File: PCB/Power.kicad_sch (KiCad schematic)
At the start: 23 parts, among them J9 USB_C_Receptacle_USB2.0_16P, SW2 SW_Push, U1 TLV62569ADRL, U4 CP2102N-Axx-xQFN28

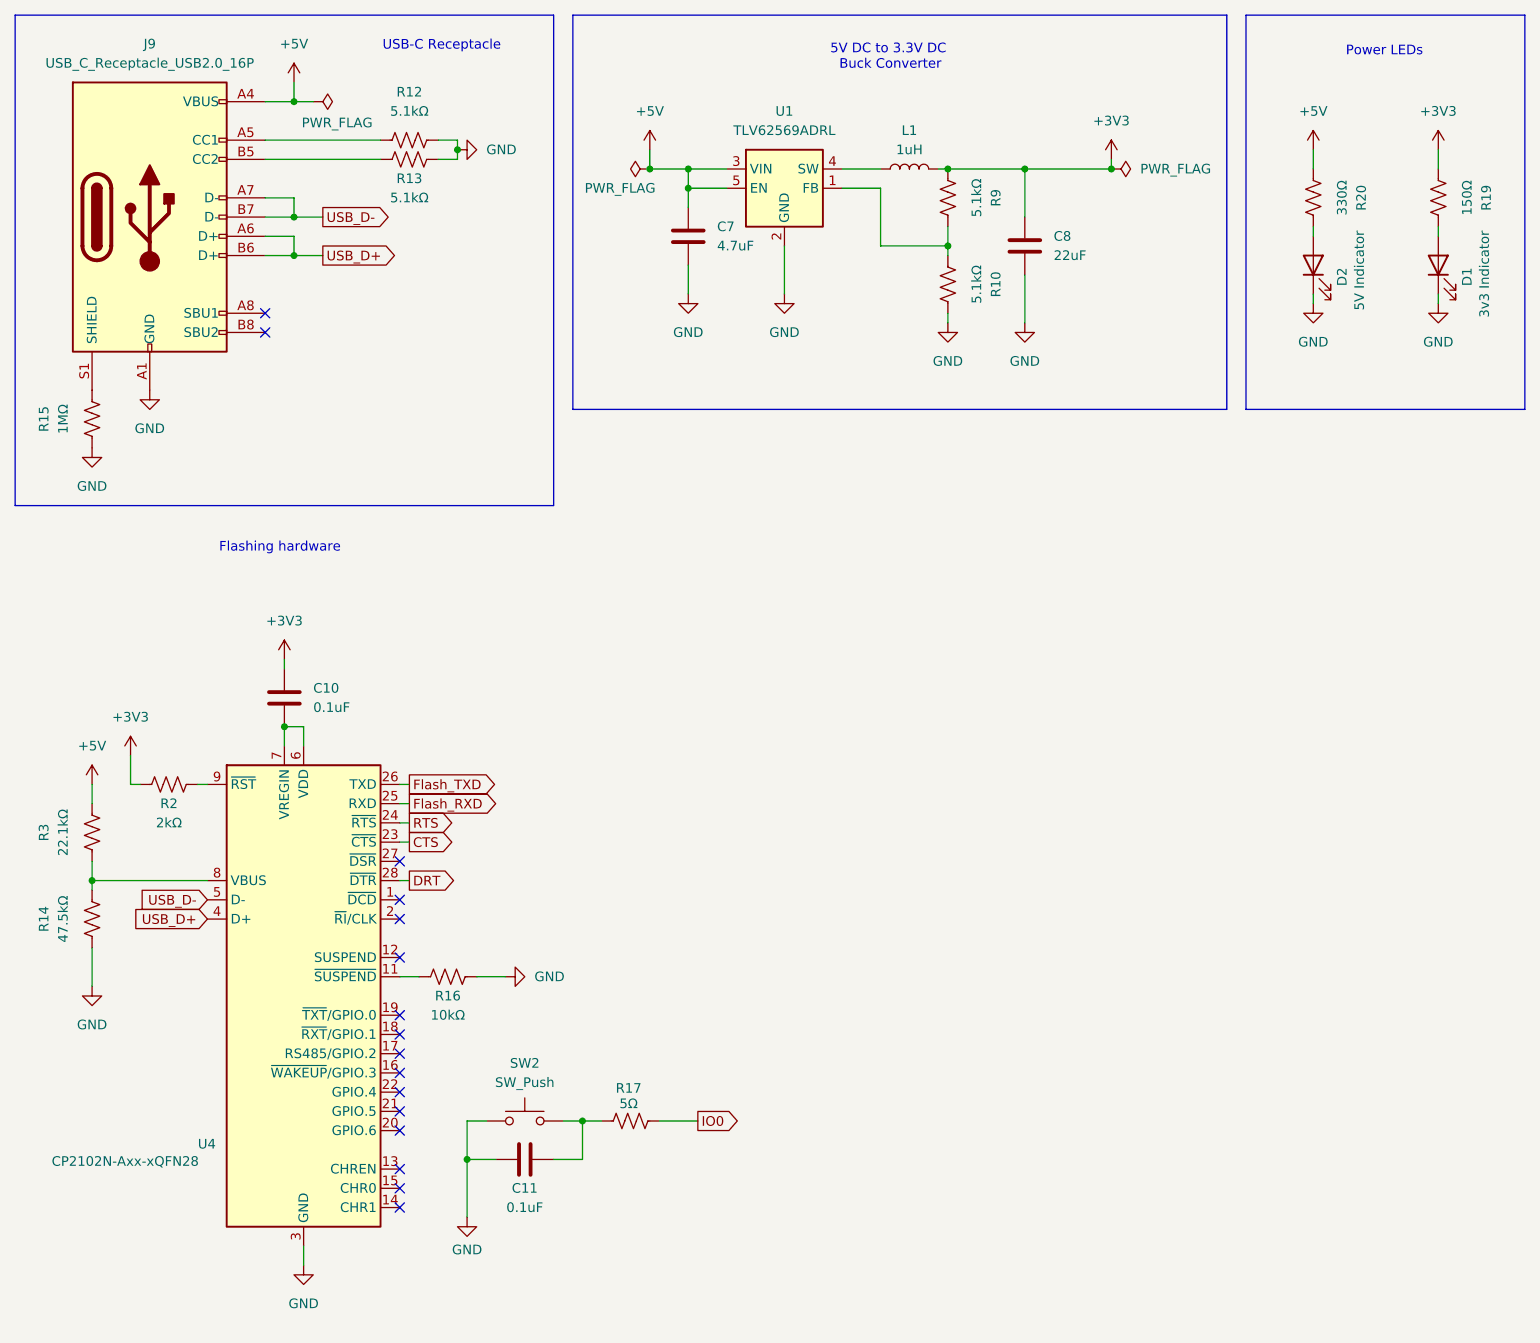
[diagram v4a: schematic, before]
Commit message: add esd protection and buck caps and move USB-C over edge
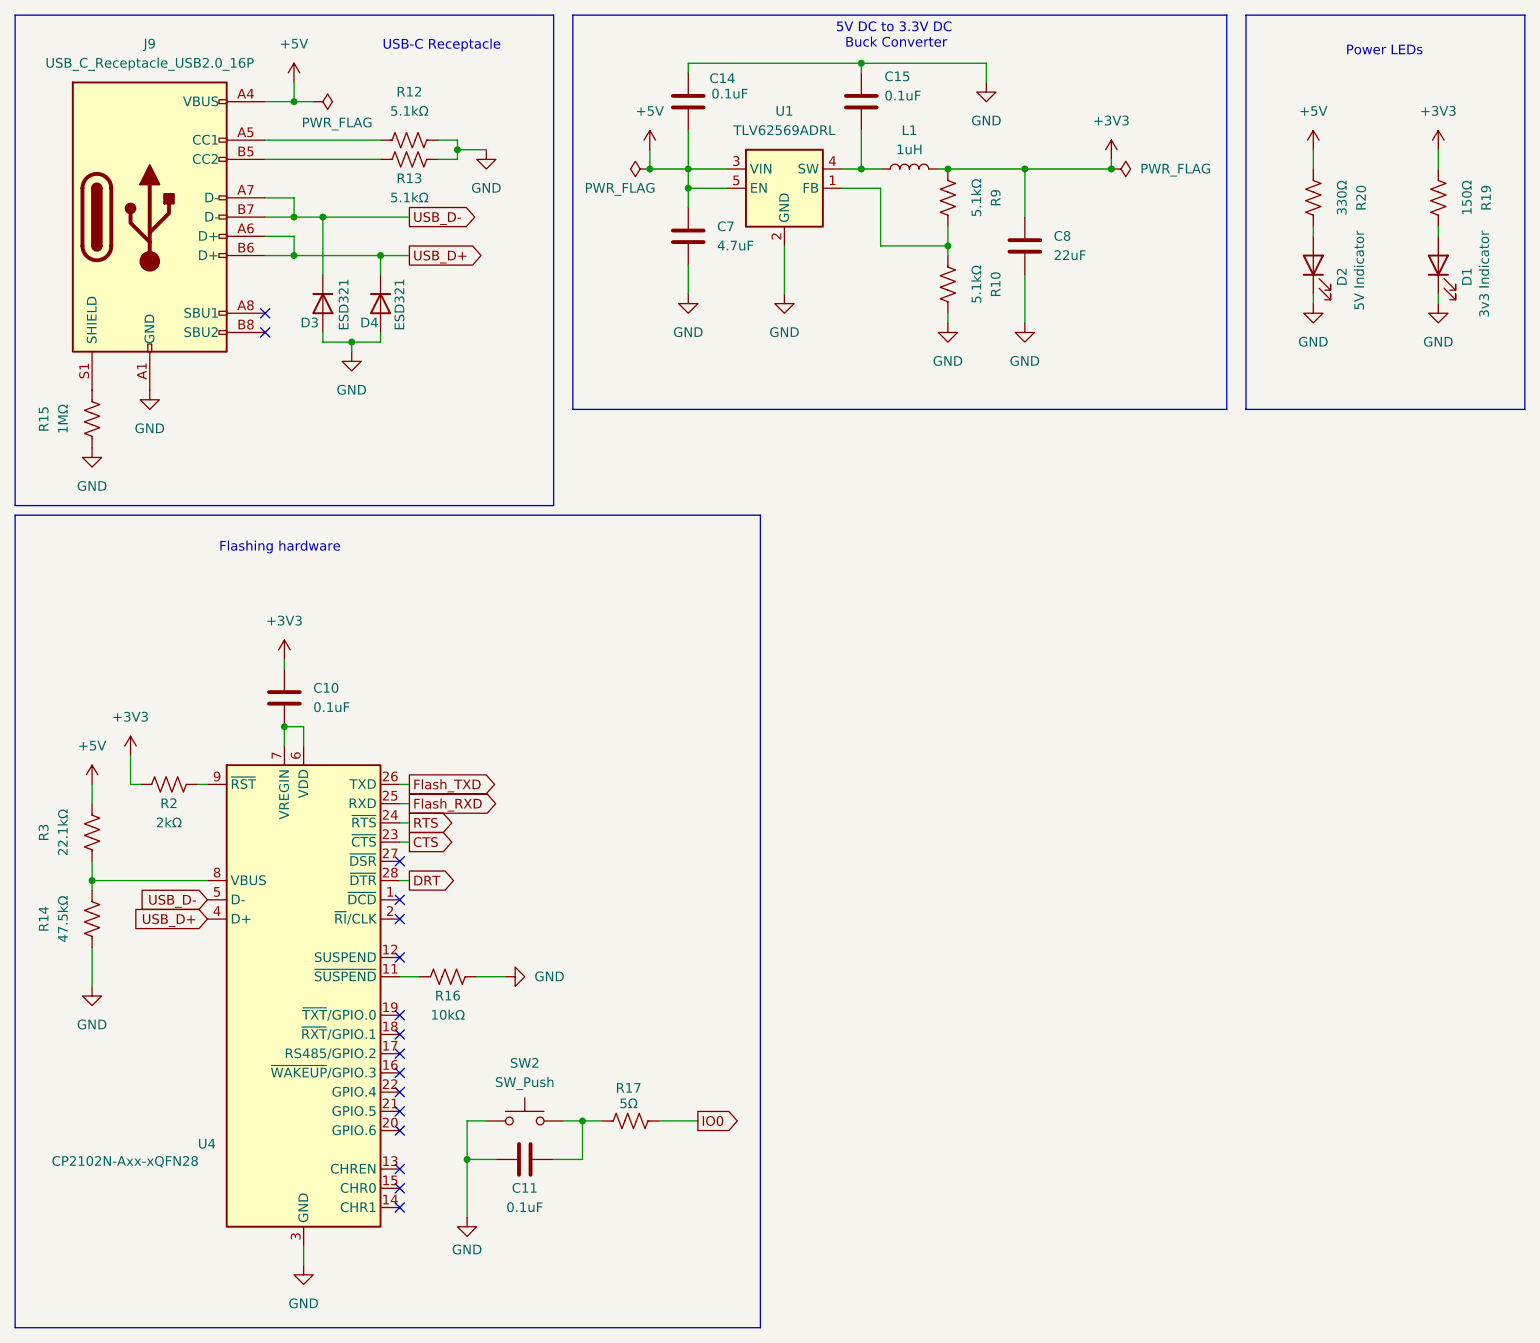
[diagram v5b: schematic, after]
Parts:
- added C14, C15: 0.1uF, Capacitor_SMD:C_1206_3216Metric_Pad1.33x1.80mm_HandSolder, symbol Device:C
- added D3, D4: ESD321, Diode_SMD:D_01005_0402Metric_Pad0.57x0.30mm_HandSolder, symbol Device:D
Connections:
- net +5V: now also C14.2
- net GND: now also C14.1, C15.1, D3.2 (A), D4.2 (A)
- net USB_D+: now also D4.1 (K)
- net USB_D-: now also D3.1 (K)
- net at L1.1, U1.4 (SW): now also C15.2

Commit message: fix esd diode footprints
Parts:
- D3, D4: footprint Diode_SMD:D_01005_0402Metric_Pad0.57x0.30mm_HandSolder -> Diode_SMD:D_0402_1005Metric_Pad0.77x0.64mm_HandSolder
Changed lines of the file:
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@@
 			)
 		)
-		(property "Footprint" "Diode_SMD:D_01005_0402Metric_Pad0.57x0.30mm_HandSolder"
+		(property "Footprint" "Diode_SMD:D_0402_1005Metric_Pad0.77x0.64mm_HandSolder"
 			(at 54.61 52.07 0)
 			(effects
@@
 			)
 		)
-		(property "Footprint" "Diode_SMD:D_01005_0402Metric_Pad0.57x0.30mm_HandSolder"
+		(property "Footprint" "Diode_SMD:D_0402_1005Metric_Pad0.77x0.64mm_HandSolder"
 			(at 62.23 52.07 0)
 			(effects

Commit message: Start of feedback implementation
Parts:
- removed C10, C11, C14, C15: 0.1uF, Capacitor_SMD:C_1206_3216Metric_Pad1.33x1.80mm_HandSolder, symbol Device:C
- removed R14: 47.5kΩ, Resistor_SMD:R_1206_3216Metric_Pad1.30x1.75mm_HandSolder, symbol Device:R_US
- removed R16: 10kΩ, Resistor_SMD:R_1206_3216Metric_Pad1.30x1.75mm_HandSolder, symbol Device:R_US
- removed R17: 5Ω, Resistor_SMD:R_1206_3216Metric_Pad1.30x1.75mm_HandSolder, symbol Device:R_US
- removed R2: 2kΩ, Resistor_SMD:R_1206_3216Metric_Pad1.30x1.75mm_HandSolder, symbol Device:R_US
- removed R3: 22.1kΩ, Resistor_SMD:R_1206_3216Metric_Pad1.30x1.75mm_HandSolder, symbol Device:R_US
- removed SW2: SW_Push, SMD_Button:Shop_SMD_Button, symbol Switch:SW_Push
- removed U4: CP2102N-Axx-xQFN28, Package_DFN_QFN:QFN-28-1EP_5x5mm_P0.5mm_EP3.35x3.35mm, symbol Interface_USB:CP2102N-Axx-xQFN28
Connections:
- no-connect marks 16 -> 2
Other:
- note removed: "Flashing hardware"
